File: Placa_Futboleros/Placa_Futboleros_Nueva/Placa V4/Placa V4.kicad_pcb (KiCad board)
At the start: 2 copper layers, 100 x 70 mm, 24 parts, among them J1 LiPo, J2 MI_Ad, J3 MI_At, J4 MD_Ad, J5 MD_At, J6 Pilas, U1 ESP32_30p, U2 DRV8833, U3 DRV8833, U5 ACS712

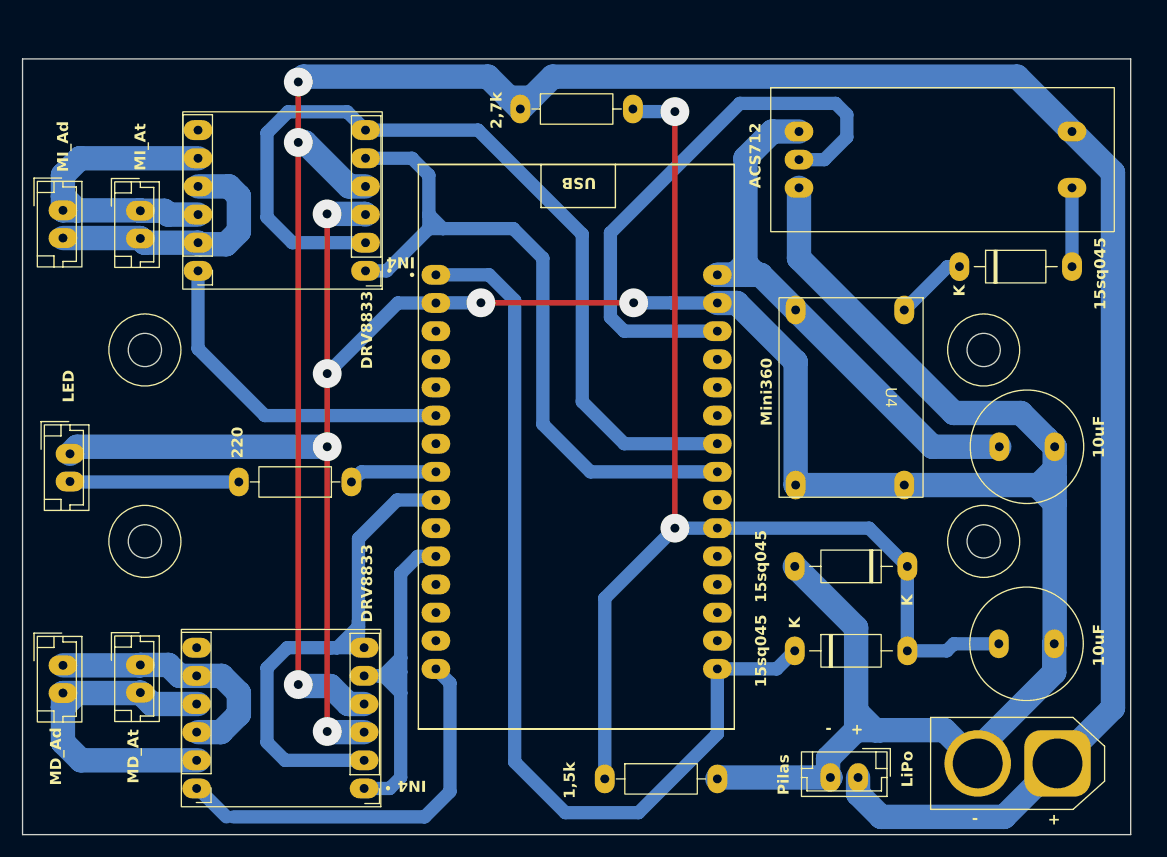
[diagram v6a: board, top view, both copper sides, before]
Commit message: Actualziación placa V4
Actualizamos sensor de corriente por sensibilidad de medicion
de ACS172 a INA219 colocando 4 resistencias SMD de 0,22 a 1W
para soportar mayor corriente a igual resolución.

Se reacomodan cosas en la placa para colocar dicho módulo.
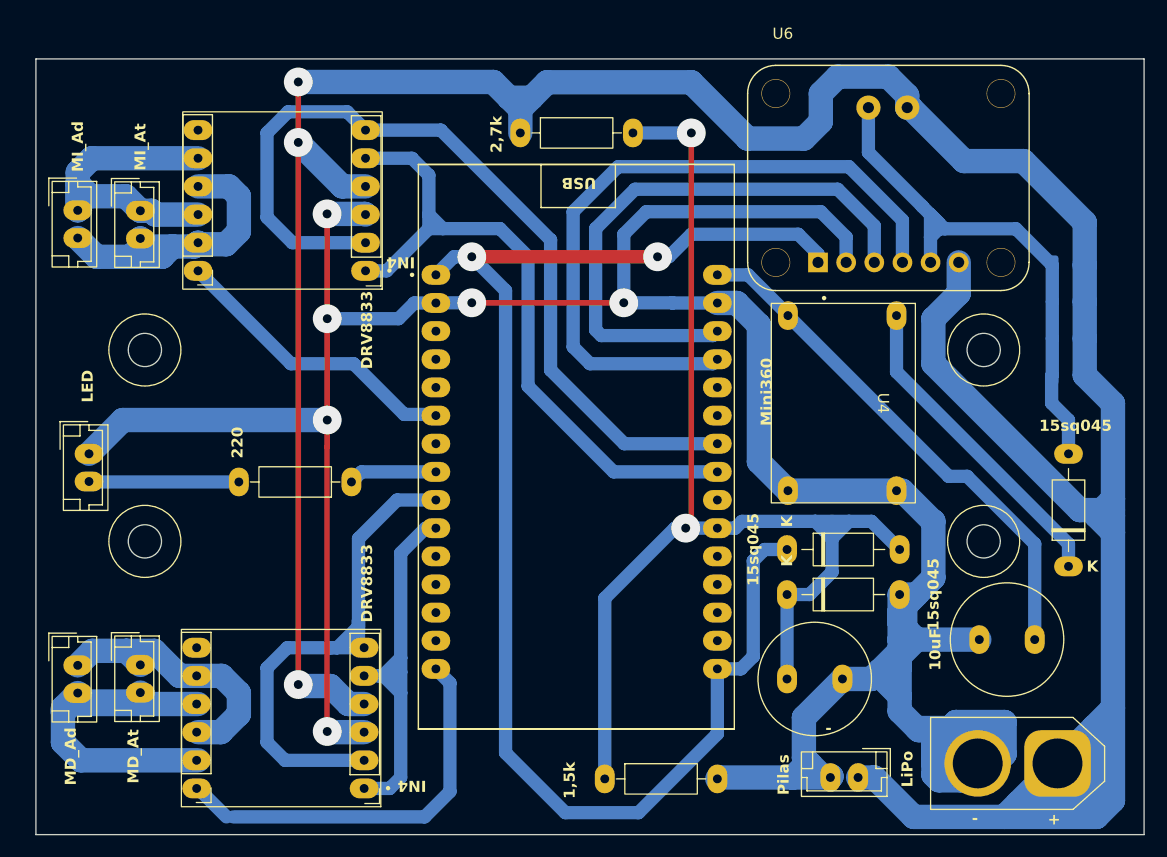
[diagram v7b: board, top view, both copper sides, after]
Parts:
- removed U5: ACS712, SensorCorriente:SensorCorr
- added R10: 0,22, Resistor_SMD:R_1206_3216Metric, B.Cu at (133.9, 55.6)
- added R7: 0,22, Resistor_SMD:R_1206_3216Metric, B.Cu at (133.9, 45.7)
- added R8: 0,22, Resistor_SMD:R_1206_3216Metric, B.Cu at (133.9, 49.0)
- added R9: 0,22, Resistor_SMD:R_1206_3216Metric, B.Cu at (133.9, 52.3)
- added U6: 904, INA219:MODULE_904, F.Cu at (104.9, 48.0)
- moved D1 28.8 mm to (133.9, 72.8), turned to 90 degrees
- moved C6 19.4 mm to (108.5, 83.0)
- moved C5 17.7 mm to (130.8, 79.5), turned to 180 degrees
- moved D3 11.2 mm to (108.5, 75.4), turned to 0 degrees
- moved D2 9.17 mm to (108.5, 71.3)
- moved R2 2.16 mm to (84.4, 33.7)
- moved D4 1.72 mm to (45.5, 62.7)
- moved J2 1.34 mm to (44.5, 40.7)
- moved J4 1.34 mm to (44.5, 81.8)
- moved U4 0.86 mm to (113.6, 58.1)
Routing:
- net VCC: track 228.2 -> 299.2 mm
- net SDA: track 0.00 -> 63.2 mm
- net SCL: track 0.00 -> 51.8 mm
- net Corriente_ADC: track 51.6 -> 0.00 mm
- net 3V3: track 86.4 -> 129.5 mm, vias 0 -> 2
- net Net-(D1-A): track 7.11 -> 50.0 mm
- net Net-(D1-K): track 6.60 -> 29.1 mm
- net GND: track 278.9 -> 290.2 mm
- net Net-(J4-Pin_2): track 31.7 -> 38.3 mm
- net 5V: track 52.9 -> 47.4 mm
- net Net-(J2-Pin_2): track 23.8 -> 29.1 mm
- net /ADC: track 105.3 -> 109.4 mm
- net SLEEP_M1: track 31.0 -> 26.9 mm
- net IN_M2A: track 34.1 -> 36.2 mm
- net IN_M1B: track 80.1 -> 78.2 mm
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
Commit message: Achico placa V4 disposición
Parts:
- removed U6: 904, INA219:MODULE_904
- added R4: 3k3, Resistor_THT:R_Axial_DIN0207_L6.3mm_D2.5mm_P10.16mm_Horizontal, F.Cu at (111.5, 36.8)
- added R5: 3k3, Resistor_THT:R_Axial_DIN0207_L6.3mm_D2.5mm_P10.16mm_Horizontal, F.Cu at (115.6, 36.8)
- added U5: INA219AxD, Package_SO:SOIC-8_3.9x4.9mm_P1.27mm, B.Cu at (122.7, 42.4)
- moved R2 31.2 mm to (115.6, 32.7), turned to 180 degrees
- moved J3 2.75 mm to (50.1, 43.5)
- moved U2 2.75 mm to (62.6, 32.7)
- moved J2 2.75 mm to (44.5, 43.5)
- moved R7 0.99 mm to (134.8, 45.9)
- moved R10 0.95 mm to (134.8, 55.6)
- moved R8 0.95 mm to (134.8, 49.0)
- moved R9 0.95 mm to (134.8, 52.3)
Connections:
- U1 pad 27: SDA -> SCL
- U1 pad 28: SCL -> SDA
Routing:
- net GND: track 290.2 -> 344.4 mm, vias 6 -> 8
- net Net-(D1-A): track 50.0 -> 26.4 mm
- net 3V3: track 129.5 -> 148.0 mm
- net SDA: track 63.2 -> 53.0 mm
- net SCL: track 51.8 -> 61.4 mm
- net VCC: track 299.2 -> 293.5 mm
- net 5V: track 47.4 -> 51.9 mm
- net /ADC: track 109.4 -> 110.7 mm
- net IN_M1B: track 78.2 -> 77.0 mm
- net SLEEP_M1: track 26.9 -> 25.7 mm
- net IN_M1A: track 62.2 -> 61.4 mm
